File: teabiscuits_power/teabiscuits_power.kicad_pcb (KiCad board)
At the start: 2 copper layers, 104 x 50.2 mm, 35 parts, among them J1 DIN-5, J10 Conn_01x03, J11 Conn_01x03, J12 Conn_01x03, J13 Conn_01x03, J14 Conn_01x03, J15 Conn_01x03, J16 Conn_01x03, J17 Conn_01x03, J18 Conn_01x03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

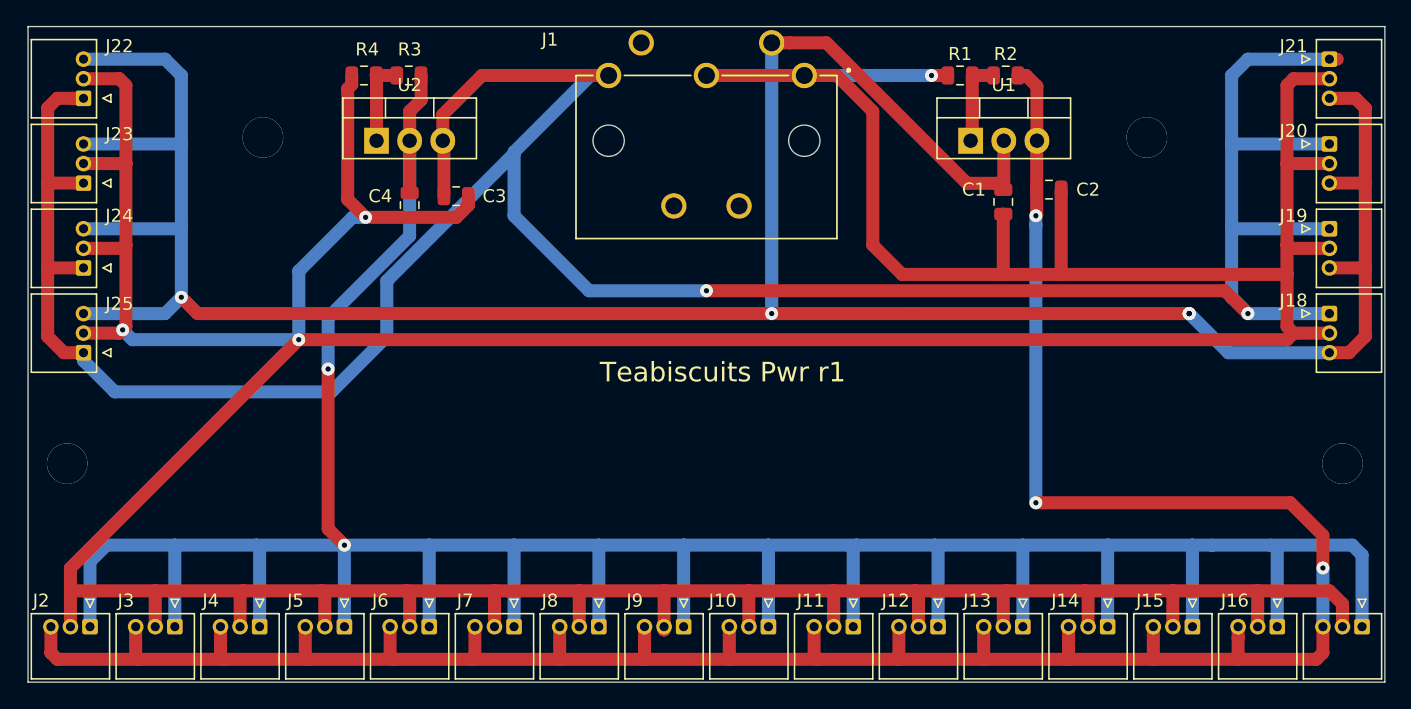
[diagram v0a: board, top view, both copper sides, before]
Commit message: Revised electrode interface (bigger holes) and power (connector was wrong way round)
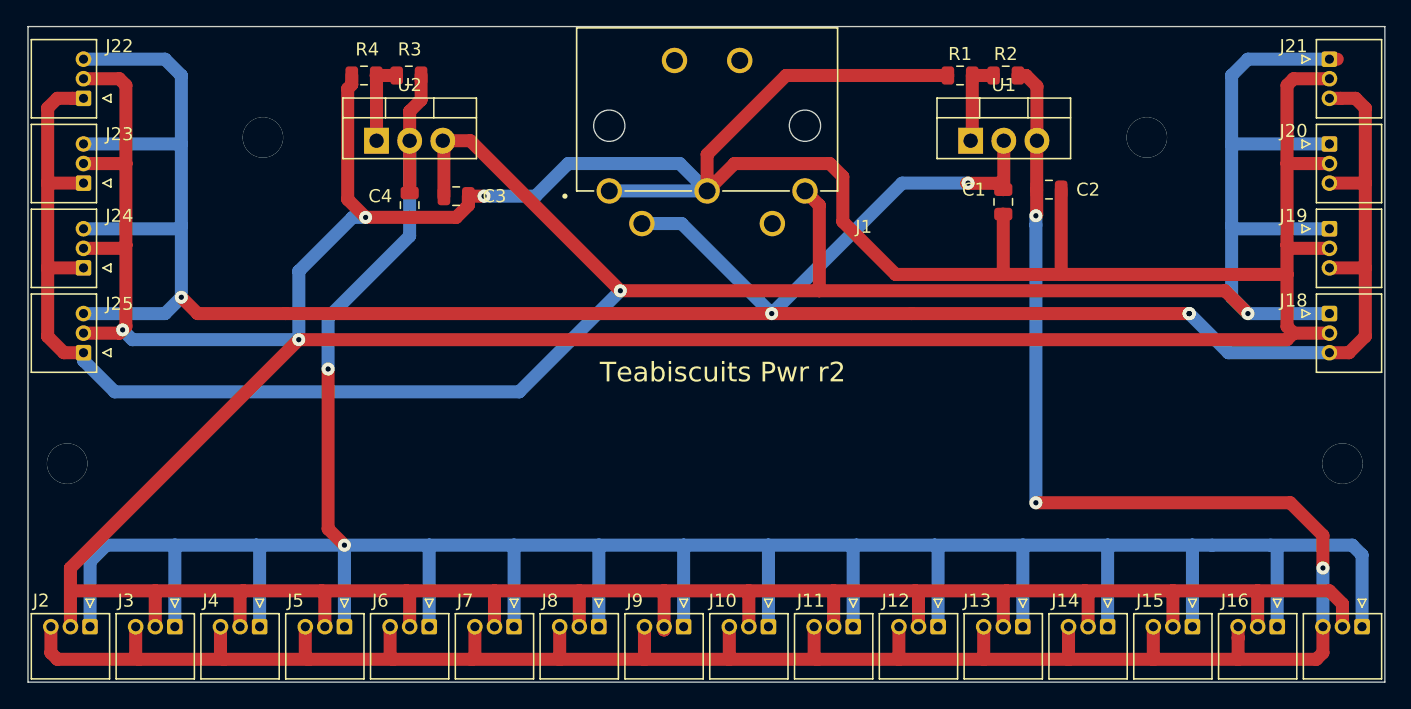
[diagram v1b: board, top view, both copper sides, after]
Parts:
- moved J1 8.85 mm to (151.1, 79.3), turned to 180 degrees
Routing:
- net GND: track 434.5 -> 469.0 mm
- net +5V: track 216.9 -> 203.6 mm
- net -5V: track 213.8 -> 205.7 mm, vias 4 -> 5
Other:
- board text added: "Teabiscuits Pwr r2"
- board text removed: "Teabiscuits Pwr r1"
